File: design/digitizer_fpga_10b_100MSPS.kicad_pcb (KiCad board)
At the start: 4 copper layers, 125 x 60 mm, 284 parts, among them J1 POWER, J2 SWD_01X04, J3 DEBUG_SPI, J4 USB_B_Mini, J5 SMA, J6 JUMPER_DFS/GAIN, J7 DEBUG_FPGA_GPIO, J8 DIGILENT_JTAG_HS2_01X06, SW1 RST, SW2 PROG, U1 LM3880MF-1AA, U10 IS61WV12816EDBLL-10TLI, U11 TLV431ACDBZR, U12 AD9214, U13 XC7S15-FTGB196, U14 IS25LP064A-JKx, U2 NCP59744MN1, U3 NCP59744MN1, U4 NCP59744MN1, U5 NCP59744MN1, U6 STM32H750VBTx, U7 USBLC6-2SC6, U8 FT231XS, U9 ADA4930-1, X1 ASTX-H11-25.000MHZ-T

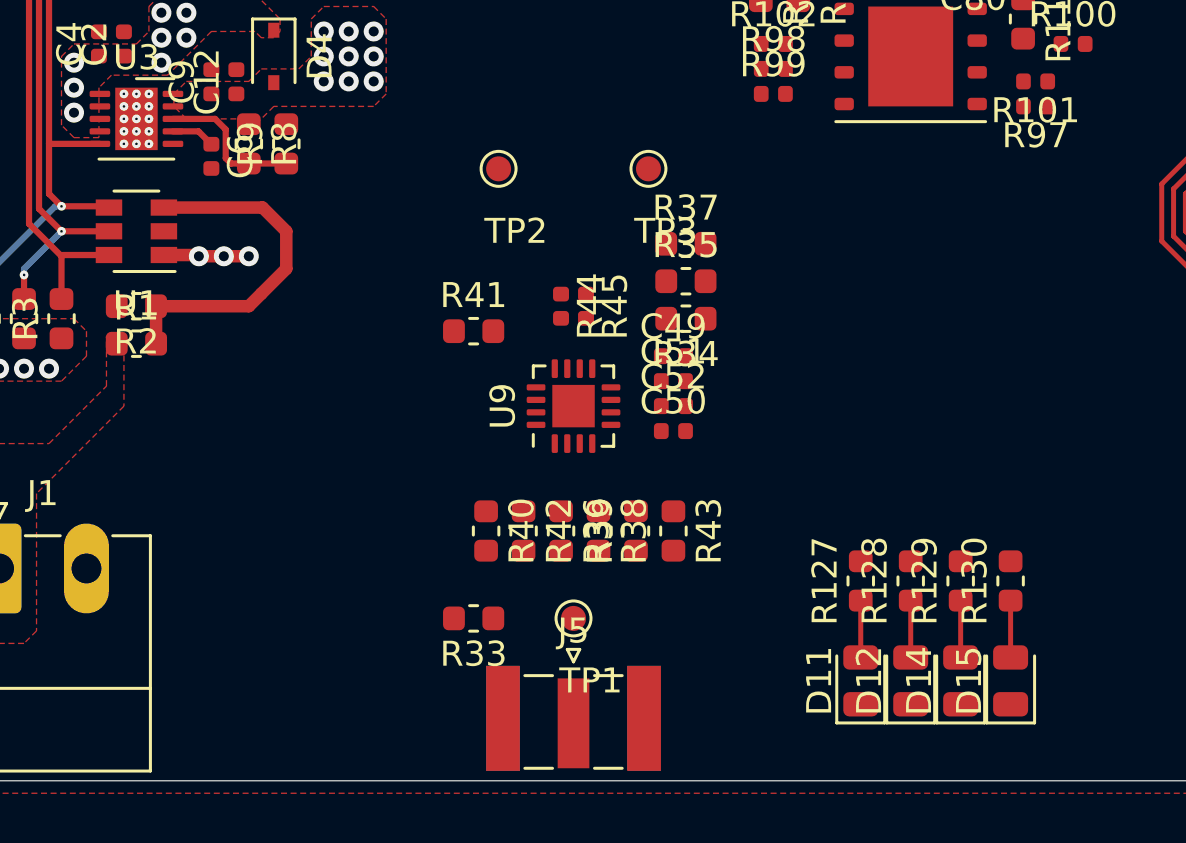
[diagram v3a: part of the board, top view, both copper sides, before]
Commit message: Moved ADC
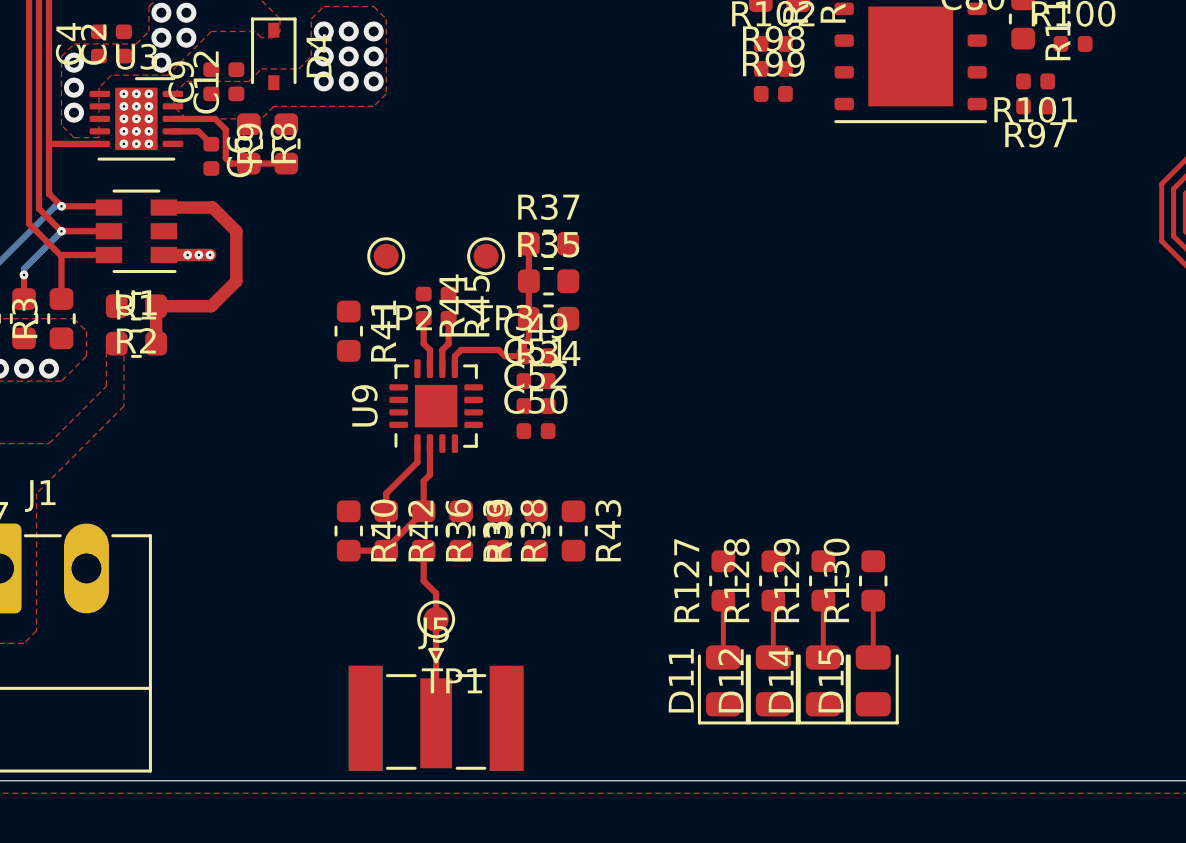
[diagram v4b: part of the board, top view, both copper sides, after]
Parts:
- moved TP3 7.38 mm to (102.0, 129.0)
- moved TP2 5.70 mm to (98.0, 129.0)
- moved TP1 5.50 mm to (100.0, 143.5)
- moved C49 5.50 mm to (104.0, 133.0)
- moved C50 5.50 mm to (104.0, 136.0)
- moved C51 5.50 mm to (104.0, 134.0)
- moved C52 5.50 mm to (104.0, 135.0)
- moved D11 5.50 mm to (111.5, 146.0)
- moved D12 5.50 mm to (113.5, 146.0)
- moved D14 5.50 mm to (115.5, 146.0)
- moved D15 5.50 mm to (117.5, 146.0)
- moved J5 5.50 mm to (100.0, 147.5)
- moved R127 5.50 mm to (111.5, 142.0)
- moved R128 5.50 mm to (113.5, 142.0)
- moved R129 5.50 mm to (115.5, 142.0)
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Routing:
- net Net-(C49-Pad1): track 0.00 -> 8.05 mm
- net /LNA/IN: track 0.00 -> 7.12 mm
- net Net-(R36-Pad1): track 0.00 -> 6.51 mm
- net Net-(R1-Pad2): track 14.1 -> 10.4 mm
- net Net-(R42-Pad1): track 0.00 -> 3.23 mm
- net Net-(R45-Pad2): track 0.00 -> 2.12 mm
- net Net-(R44-Pad2): track 0.00 -> 2.12 mm
- net IN: track 3.42 -> 1.85 mm

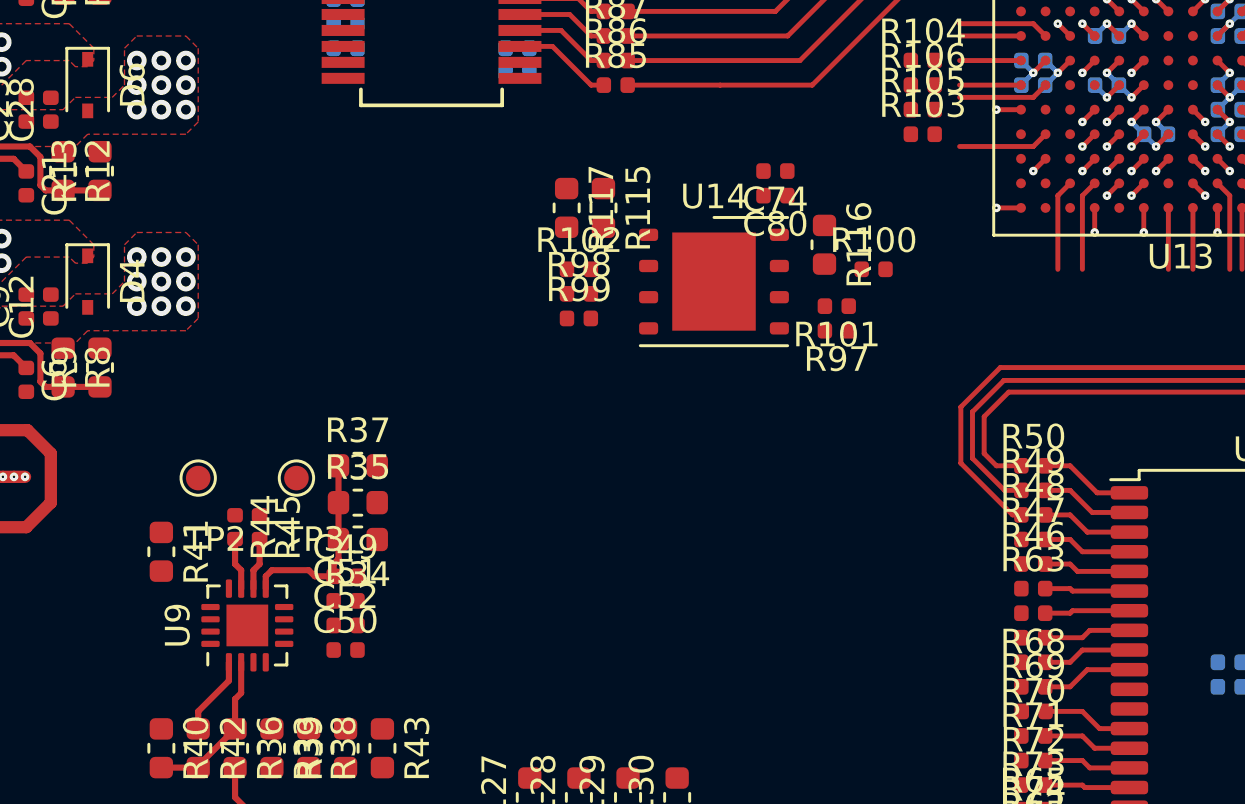
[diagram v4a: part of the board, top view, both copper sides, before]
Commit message: Updated FLASH placement
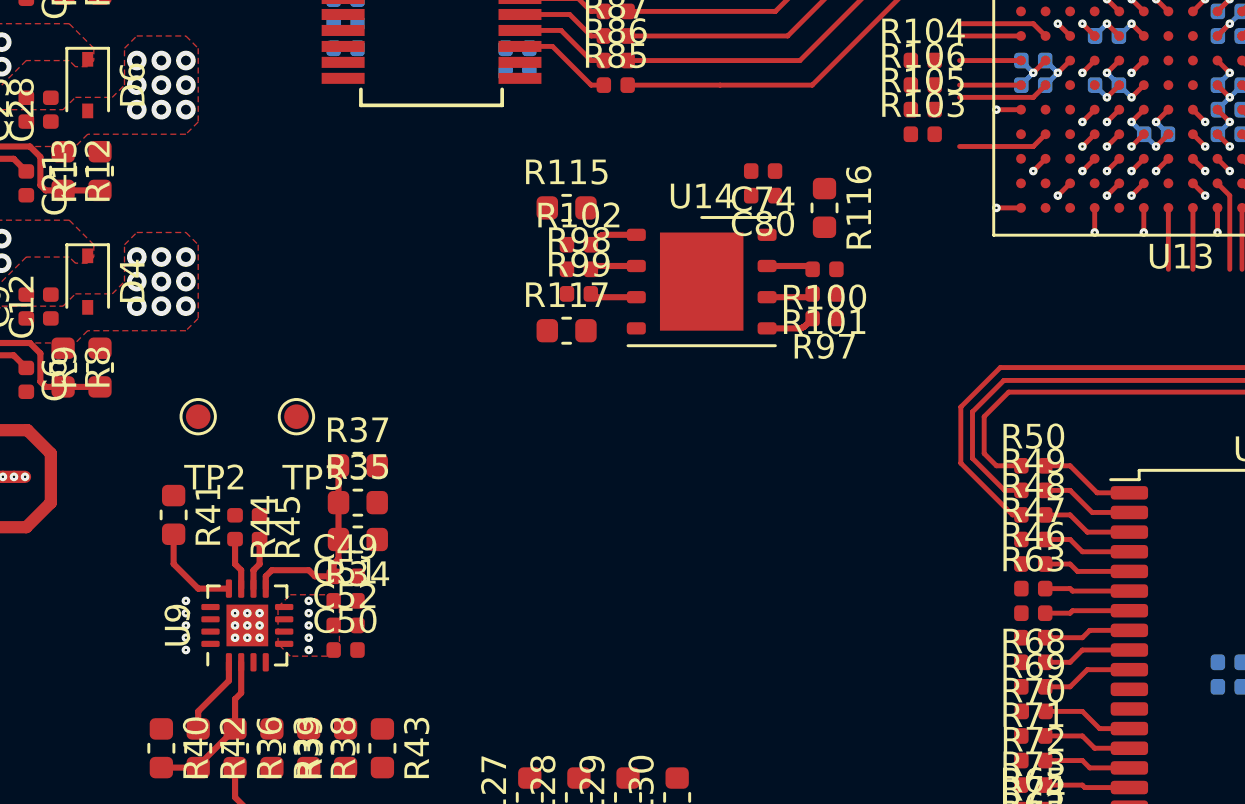
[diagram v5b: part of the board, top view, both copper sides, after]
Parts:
- moved R117 5.00 mm to (113.0, 123.0), turned to 0 degrees
- moved TP2 2.50 mm to (98.0, 126.5)
- moved TP3 2.50 mm to (102.0, 126.5)
- moved R100 2.00 mm to (123.5, 120.5), turned to 180 degrees
- moved R41 1.58 mm to (97.0, 130.5)
- moved R115 1.50 mm to (113.0, 118.0), turned to 0 degrees
- moved R116 1.50 mm to (123.5, 118.0)
- moved R102 1.00 mm to (113.5, 119.5)
- moved R98 1.00 mm to (113.5, 120.5)
- moved R99 1.00 mm to (113.5, 121.5)
- moved R101 0.71 mm to (123.5, 121.5)
- moved R97 0.71 mm to (123.5, 122.5)
- moved C74 0.50 mm to (121.0, 116.5)
- moved C80 0.50 mm to (121.0, 117.5)
- moved U14 0.50 mm to (118.5, 121.0)
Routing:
- net Net-(R41-Pad2): track 0.00 -> 3.88 mm
- net /FPGA/FPGA_DQ0: track 3.71 -> 0.00 mm
- net /FPGA/FPGA_DQ1: track 3.71 -> 0.71 mm, vias 0 -> 1
- net Net-(R102-Pad2): track 0.00 -> 2.00 mm
- net Net-(R97-Pad2): track 0.00 -> 2.00 mm
- net Net-(R98-Pad2): track 0.00 -> 1.90 mm
- net Net-(R117-Pad2): track 0.00 -> 1.90 mm
- net Net-(R100-Pad2): track 0.00 -> 1.90 mm
- net Net-(R101-Pad2): track 0.00 -> 1.90 mm
- net GND: vias 115 -> 129
- net +3V3A: vias 9 -> 14

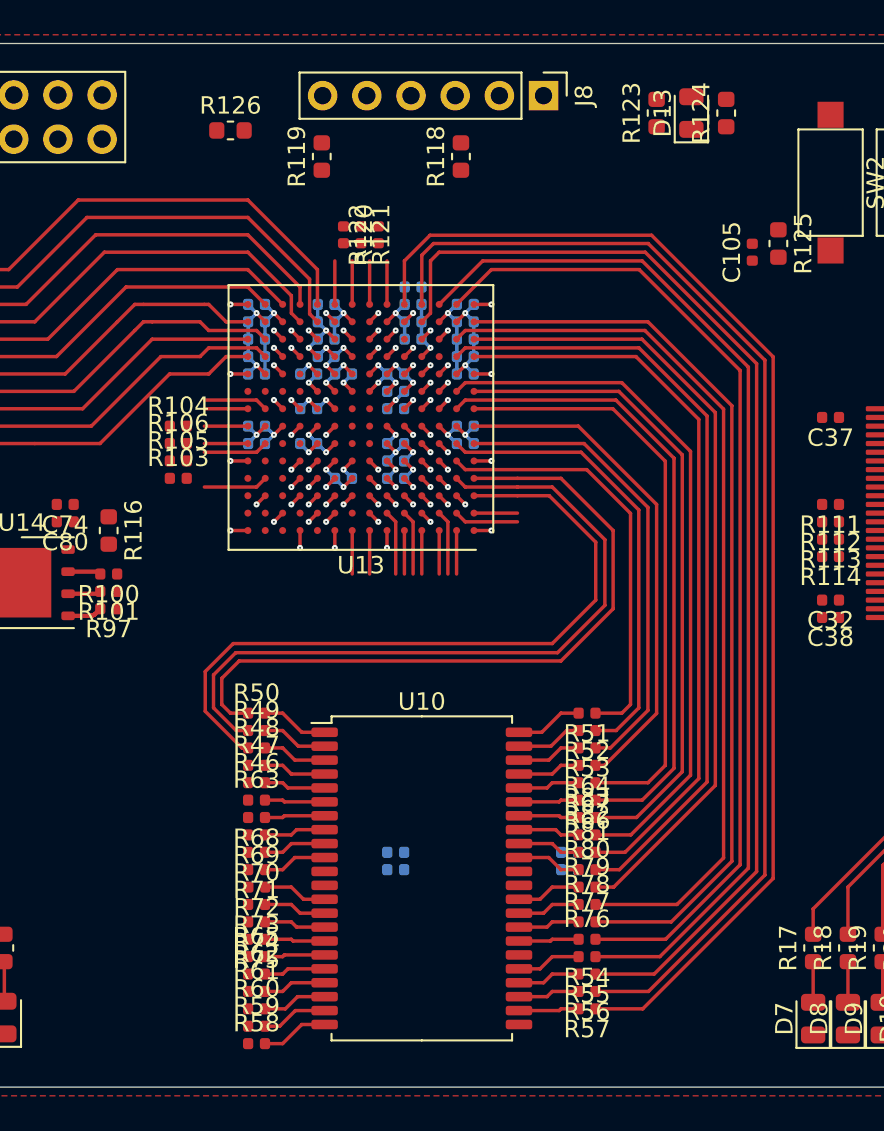
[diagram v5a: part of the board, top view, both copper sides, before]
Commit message: Chenged Rs positions
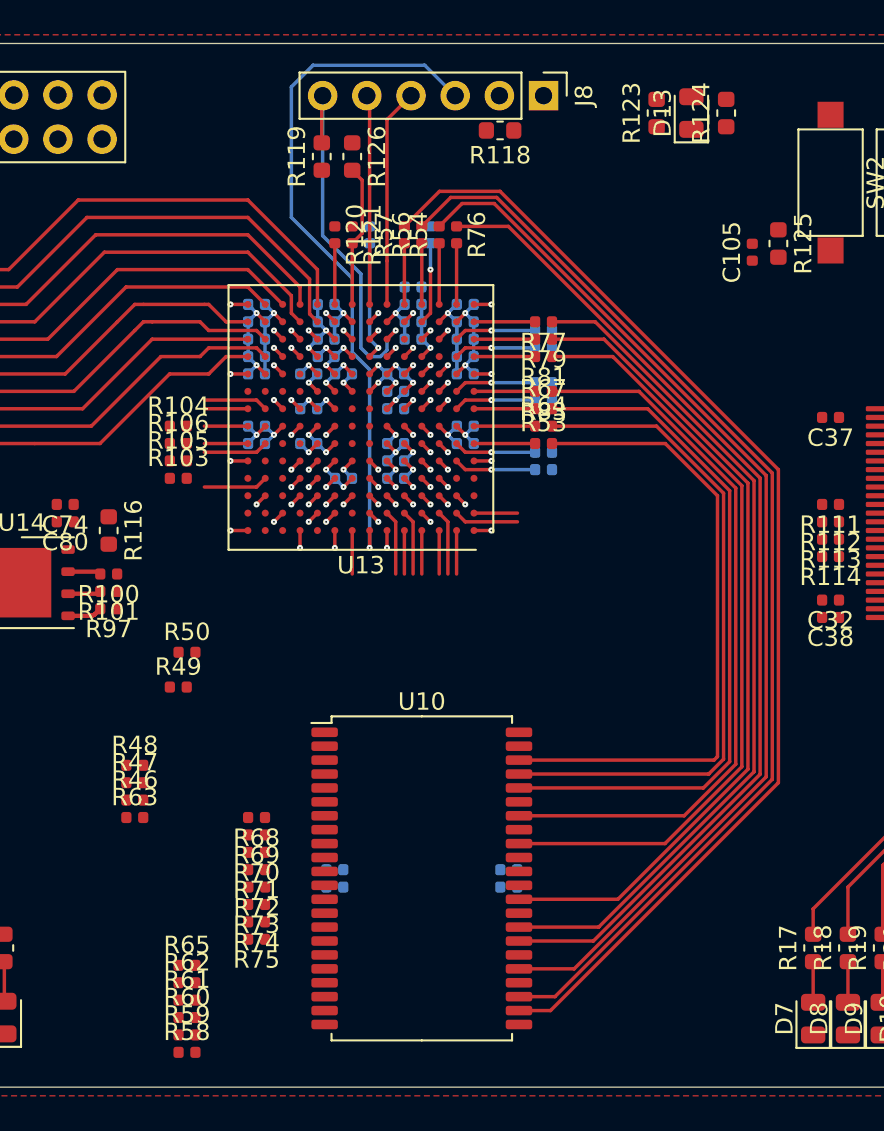
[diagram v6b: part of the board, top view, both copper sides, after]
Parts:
- R122, R51, R52, R55, R66, R78, R80, R82: moved to B.Cu
- moved R57 45.7 mm to (140.5, 101.0), turned to 90 degrees
- moved R56 44.5 mm to (141.5, 101.0), turned to 90 degrees
- moved R55 43.4 mm to (142.0, 101.0), turned to 90 degrees
- moved R54 42.4 mm to (142.5, 101.0), turned to 90 degrees
- moved R76 41.2 mm to (143.5, 101.0), turned to -90 degrees
- moved R77 34.6 mm to (148.5, 106.0), turned to 180 degrees
- moved R78 33.1 mm to (148.5, 106.5), turned to 180 degrees
- moved R79 31.6 mm to (148.5, 107.0), turned to 180 degrees
- moved R80 30.1 mm to (148.5, 107.5), turned to 180 degrees
- moved R81 28.6 mm to (148.5, 108.0), turned to 180 degrees
- moved R82 26.1 mm to (148.5, 109.5), turned to 180 degrees
- moved R83 24.6 mm to (148.5, 110.0), turned to 180 degrees
- moved R66 23.1 mm to (148.5, 110.5), turned to 0 degrees
- moved R67 21.6 mm to (148.5, 111.0), turned to 0 degrees
- moved R64 19.7 mm to (148.5, 112.0), turned to 0 degrees
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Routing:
- net /SRAM_A11: track 70.5 -> 3.52 mm
- net /SRAM_A10: track 67.7 -> 3.52 mm
- net Net-(R57-Pad2): track 3.47 -> 67.3 mm
- net /SRAM_A9: track 66.2 -> 4.72 mm, vias 0 -> 1
- net Net-(R56-Pad2): track 3.55 -> 64.8 mm
- net Net-(R54-Pad2): track 3.72 -> 61.9 mm
- net /SRAM_A8: track 61.0 -> 3.52 mm
- net Net-(R76-Pad1): track 3.47 -> 58.3 mm
- net /SRAM_IO8: track 58.0 -> 3.52 mm
- net /SRAM_IO9: track 52.3 -> 3.51 mm
- net /SRAM_IO10: track 51.7 -> 4.72 mm, vias 0 -> 1
- net Net-(R77-Pad1): track 3.55 -> 49.3 mm
- net Net-(R79-Pad1): track 3.72 -> 47.4 mm
- net /SRAM_IO11: track 46.4 -> 3.51 mm
- net /SRAM_A3: track 42.3 -> 0.00 mm
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
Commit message: Added some tracks
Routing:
- net Net-(R53-Pad2): track 37.3 -> 30.0 mm
- net Net-(R81-Pad1): track 44.8 -> 41.4 mm
- net Net-(R83-Pad1): track 42.4 -> 39.0 mm
- net Net-(R77-Pad1): track 49.3 -> 45.9 mm
- net Net-(R67-Pad2): track 40.5 -> 37.1 mm
- net Net-(R79-Pad1): track 47.4 -> 44.0 mm
- net Net-(R76-Pad1): track 58.3 -> 54.9 mm
- net Net-(R64-Pad2): track 38.9 -> 35.5 mm
- net Net-(R54-Pad2): track 61.9 -> 58.9 mm
- net Net-(R56-Pad2): track 64.8 -> 62.3 mm
- net Net-(R57-Pad2): track 67.3 -> 65.6 mm

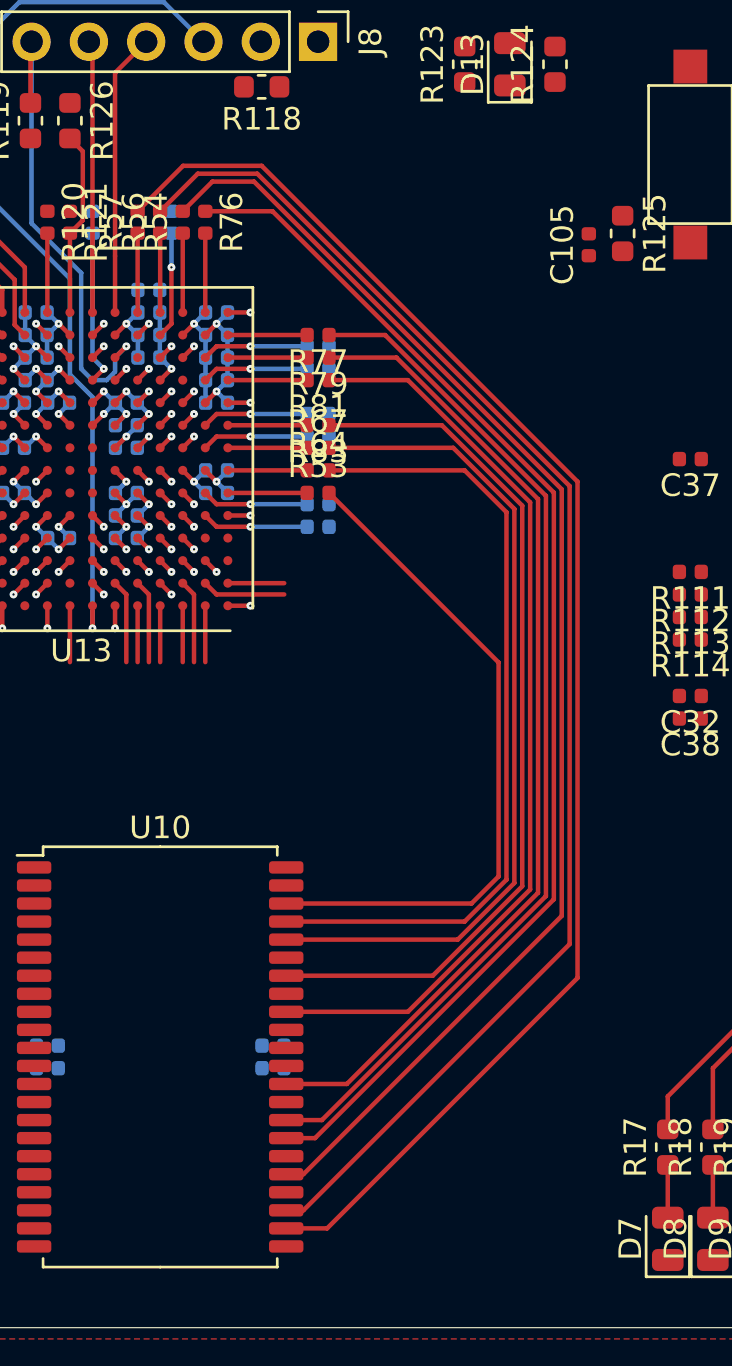
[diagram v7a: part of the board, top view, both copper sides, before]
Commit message: Added test RAM layout
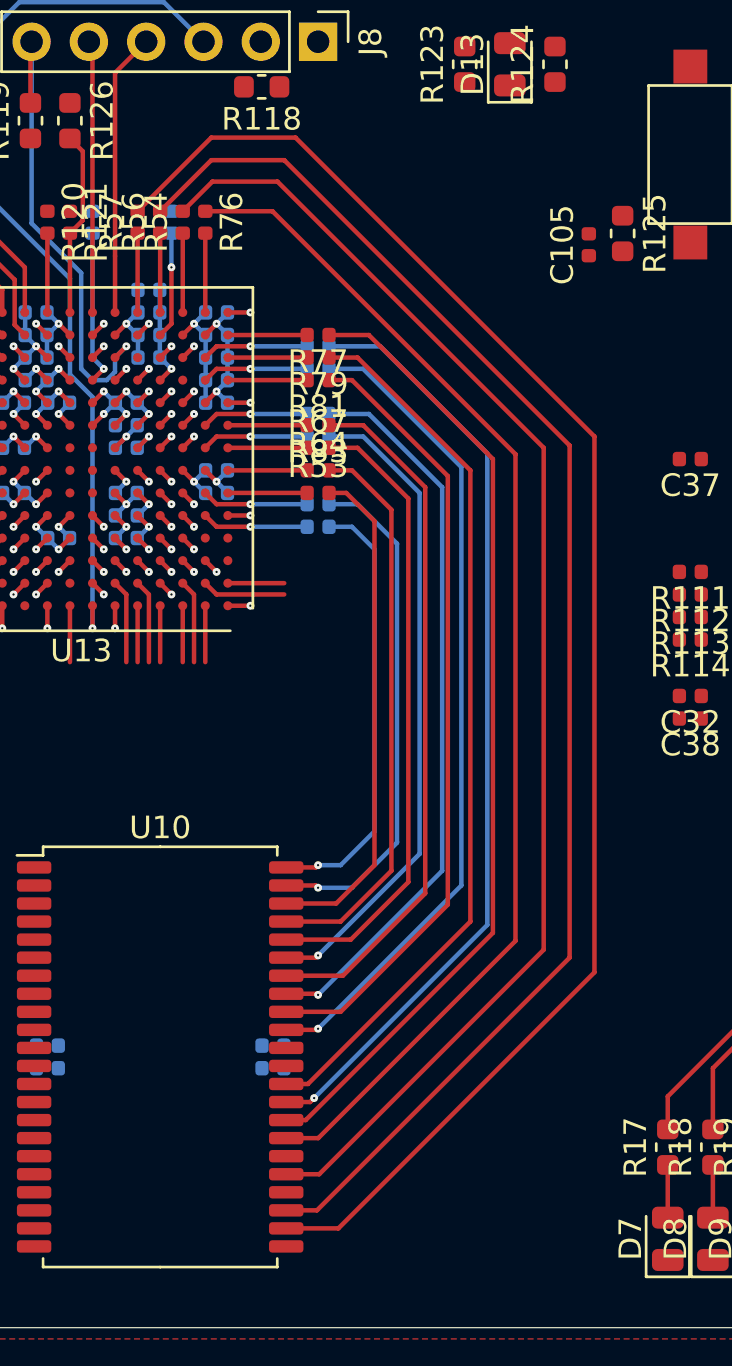
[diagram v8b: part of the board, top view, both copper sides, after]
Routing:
- net Net-(R78-Pad1): track 0.00 -> 42.0 mm, vias 0 -> 1
- net Net-(R80-Pad1): track 0.00 -> 36.6 mm, vias 0 -> 1
- net Net-(R82-Pad1): track 0.00 -> 32.6 mm, vias 0 -> 1
- net Net-(R66-Pad2): track 0.00 -> 28.9 mm, vias 0 -> 1
- net Net-(R52-Pad2): track 0.00 -> 22.8 mm, vias 0 -> 1
- net Net-(R51-Pad2): track 0.00 -> 19.5 mm, vias 0 -> 1
- net Net-(R64-Pad2): track 35.5 -> 25.1 mm
- net Net-(R67-Pad2): track 37.1 -> 27.9 mm
- net Net-(R83-Pad1): track 39.0 -> 31.1 mm
- net Net-(R53-Pad2): track 30.0 -> 22.4 mm
- net Net-(R81-Pad1): track 41.4 -> 35.2 mm
- net Net-(R79-Pad1): track 44.0 -> 39.5 mm
- net Net-(R57-Pad2): track 65.6 -> 69.2 mm
- net Net-(R77-Pad1): track 45.9 -> 43.1 mm
- net Net-(R56-Pad2): track 62.3 -> 64.2 mm
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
